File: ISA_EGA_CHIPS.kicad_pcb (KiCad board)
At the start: 2 copper layers, 131.1 x 108 mm, 67 parts, among them J1 EGA Feature Connector, J2 Light Pen, J3 RCA 1, J4 RCA 2, J6 Digital Output, J7 Bus_ISA_8bit, SW1 Configuration, U1 41464, U10 27C256, U11 82A436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

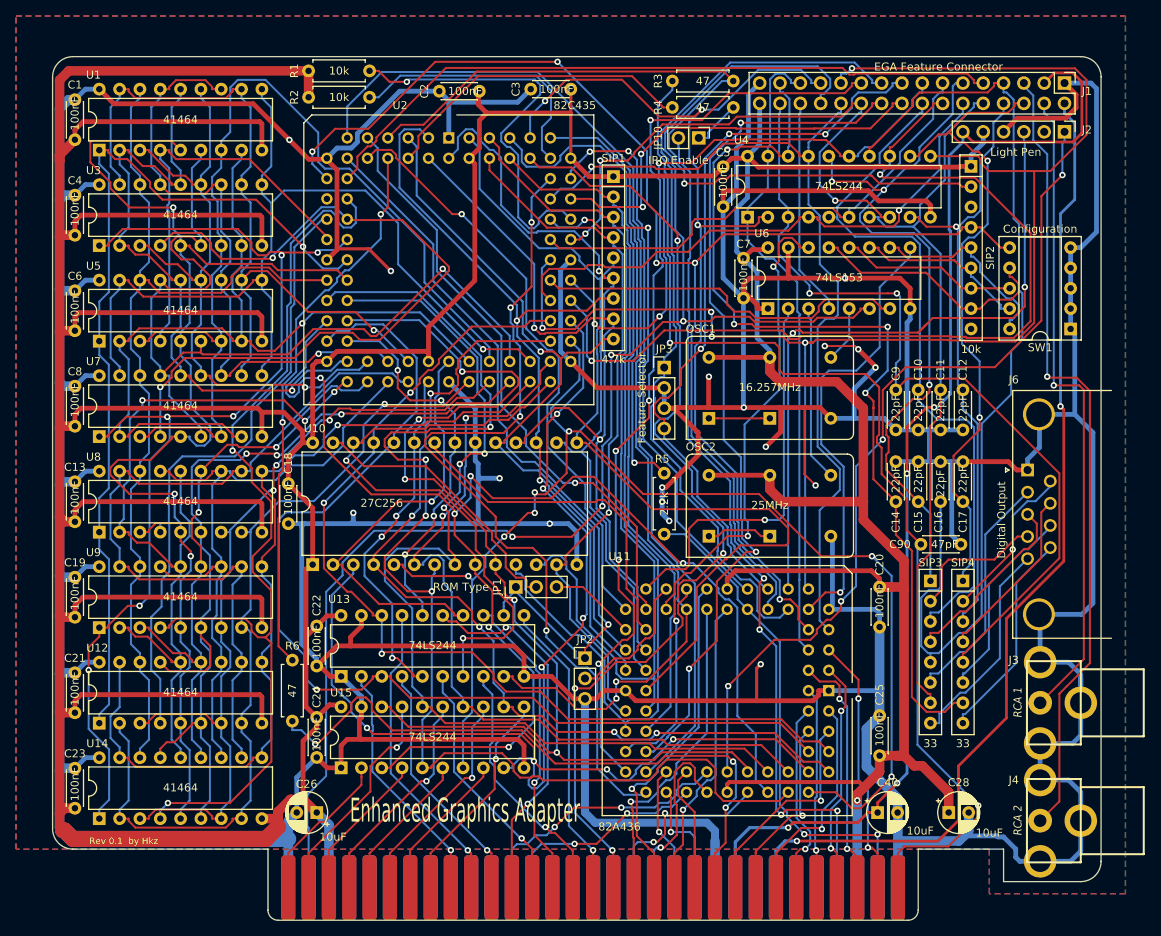
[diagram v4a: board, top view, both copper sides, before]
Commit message: Update grounding
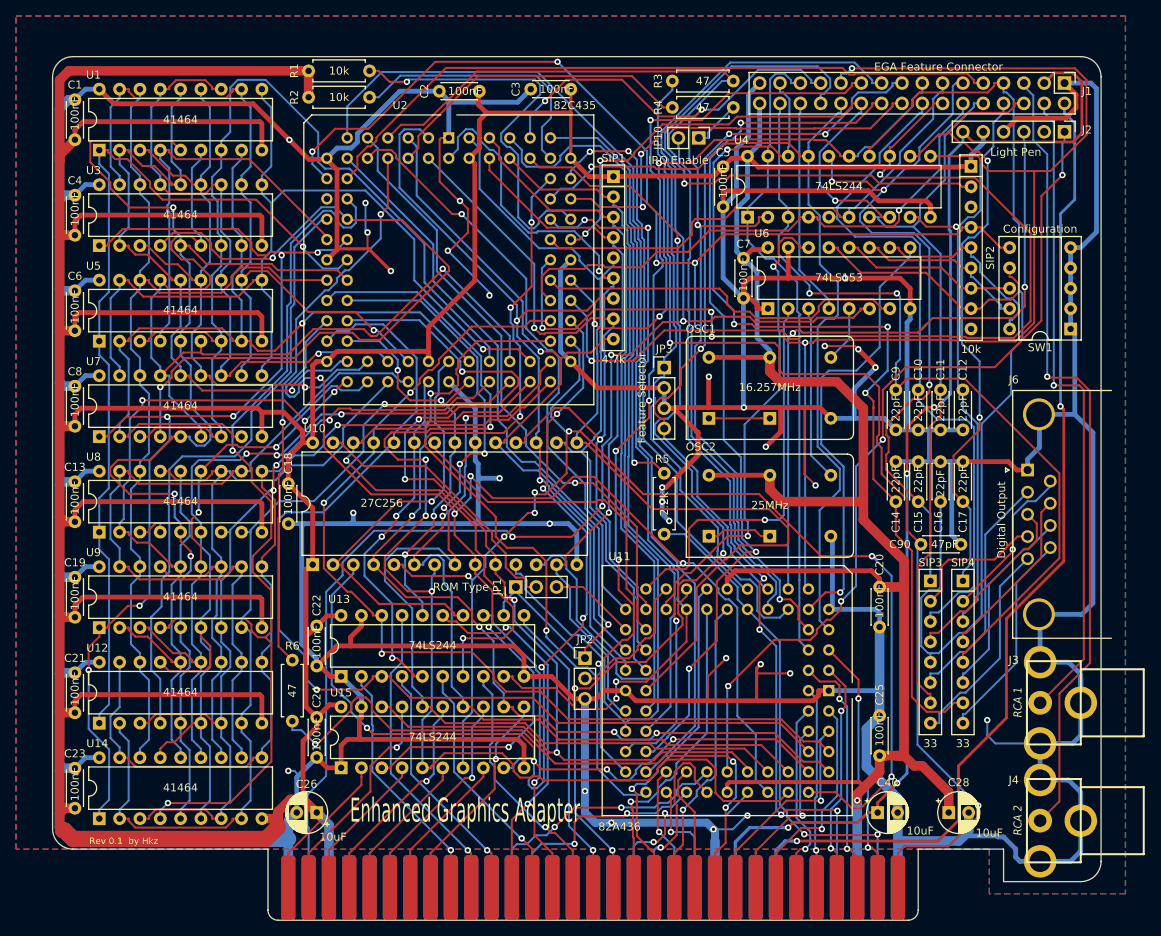
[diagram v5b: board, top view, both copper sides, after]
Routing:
- net GND: track 1036.8 -> 1094.3 mm, vias 17 -> 30
- net /~DACK0: track 26.8 -> 28.4 mm
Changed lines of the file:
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@@
     (thickness 1.6)
     (drawings 22)
-    (tracks 4128)
+    (tracks 4179)
     (zones 0)
     (modules 67)
@@
   (segment (start 243.666 99.568) (end 242.0386 101.1954) (width 0.6) (layer B.Cu) (net 1))
   (segment (start 242.0386 101.1954) (end 233.426 101.1954) (width 0.6) (layer B.Cu) (net 1))
-  (segment (start 216.916 183.104) (end 214.416 185.604) (width 0.6) (layer B.Cu) (net 1))
   (segment (start 214.416 185.604) (end 214.416 189.992) (width 0.6) (layer B.Cu) (net 1))
   (segment (start 255.524 174.752) (end 256.79 176.018) (width 0.6) (layer F.Cu) (net 1))
@@
   (segment (start 311.15 127) (end 311.15 124.46) (width 0.6) (layer B.Cu) (net 1))
   (segment (start 266.7 193.548) (end 266.7 192.278) (width 1) (layer B.Cu) (net 1))
-  (segment (start 266.7 192.278) (end 265.684 191.262) (width 1) (layer B.Cu) (net 1))
-  (segment (start 265.684 191.262) (end 251.714 191.262) (width 1) (layer B.Cu) (net 1))
+  (segment (start 266.7 192.278) (end 266.5095 192.0875) (width 1) (layer B.Cu) (net 1))
+  (segment (start 265.684 191.262) (end 253.746 191.262) (width 1) (layer B.Cu) (net 1))
   (segment (start 251.714 191.262) (end 250.444 189.992) (width 1) (layer B.Cu) (net 1))
-  (segment (start 250.444 189.992) (end 250.444 175.768) (width 1) (layer B.Cu) (net 1))
+  (segment (start 250.444 189.992) (end 250.444 187.325) (width 1) (layer B.Cu) (net 1))
   (segment (start 297.688 142.16) (end 294.894 142.16) (width 0.6) (layer B.Cu) (net 1))
   (segment (start 287.274 177.88) (end 287.274 174.498) (width 1.2) (layer B.Cu) (net 1))
@@
   (via (at 272.415 171.45) (size 0.8) (drill 0.4) (layers F.Cu B.Cu) (net 1))
   (segment (start 271.903 171.962) (end 272.415 171.45) (width 0.4) (layer F.Cu) (net 1))
-  (segment (start 271.903 176.018) (end 271.903 171.962) (width 0.4) (layer F.Cu) (net 1))
-  (segment (start 256.79 176.018) (end 271.903 176.018) (width 0.6) (layer F.Cu) (net 1))
   (segment (start 271.903 176.018) (end 278.9485 176.018) (width 0.6) (layer F.Cu) (net 1))
   (segment (start 213.4944 105.9106) (end 215.9188 108.335) (width 0.6) (layer F.Cu) (net 1))
@@
   (segment (start 277.876 139.446) (end 277.7956 139.3656) (width 0.25) (layer F.Cu) (net 1))
   (segment (start 279.8276 139.3656) (end 277.7956 139.3656) (width 0.6) (layer F.Cu) (net 1))
+  (via (at 223.266 117.475) (size 0.8) (drill 0.4) (layers F.Cu B.Cu) (net 1))
+  (segment (start 223.266 119.38) (end 223.411201 119.525201) (width 0.25) (layer F.Cu) (net 1))
+  (segment (start 223.266 117.475) (end 223.266 119.38) (width 0.25) (layer F.Cu) (net 1))
+  (via (at 223.012 113.792) (size 0.8) (drill 0.4) (layers F.Cu B.Cu) (net 1))
+  (segment (start 223.012 117.221) (end 223.266 117.475) (width 0.25) (layer B.Cu) (net 1))
+  (segment (start 223.012 113.792) (end 223.012 117.221) (width 0.25) (layer B.Cu) (net 1))
+  (segment (start 232.4648 105.664) (end 232.283 105.8458) (width 0.25) (layer F.Cu) (net 1))
+  (segment (start 233.426 105.664) (end 232.4648 105.664) (width 0.25) (layer F.Cu) (net 1))
+  (segment (start 232.283 105.8458) (end 232.283 111.125) (width 0.25) (layer F.Cu) (net 1))
+  (via (at 234.823 113.538) (size 0.8) (drill 0.4) (layers F.Cu B.Cu) (net 1))
+  (segment (start 234.696 113.538) (end 234.823 113.538) (width 0.25) (layer F.Cu) (net 1))
+  (segment (start 232.283 111.125) (end 234.696 113.538) (width 0.25) (layer F.Cu) (net 1))
+  (segment (start 235.810301 114.525301) (end 235.810301 117.503699) (width 0.25) (layer F.Cu) (net 1))
+  (segment (start 234.823 113.538) (end 235.810301 114.525301) (width 0.25) (layer F.Cu) (net 1))
+  (via (at 233.299 119.761) (size 0.8) (drill 0.4) (layers F.Cu B.Cu) (net 1))
+  (segment (start 233.553 119.761) (end 233.299 119.761) (width 0.25) (layer F.Cu) (net 1))
+  (segment (start 235.810301 117.503699) (end 233.553 119.761) (width 0.25) (layer F.Cu) (net 1))
+  (via (at 238.506 125.349) (size 0.8) (drill 0.4) (layers F.Cu B.Cu) (net 1))
+  (segment (start 238.506 124.968) (end 238.506 125.349) (width 0.25) (layer B.Cu) (net 1))
+  (segment (start 233.299 119.761) (end 238.506 124.968) (width 0.25) (layer B.Cu) (net 1))
+  (via (at 276.098 172.593) (size 0.8) (drill 0.4) (layers F.Cu B.Cu) (net 1))
+  (via (at 268.097 170.688) (size 0.8) (drill 0.4) (layers F.Cu B.Cu) (net 1))
+  (segment (start 272.026 172.593) (end 271.903 172.47) (width 0.25) (layer F.Cu) (net 1))
+  (segment (start 276.098 172.593) (end 272.026 172.593) (width 0.25) (layer F.Cu) (net 1))
+  (segment (start 271.903 172.47) (end 271.903 171.962) (width 0.4) (layer F.Cu) (net 1))
+  (segment (start 271.903 176.018) (end 271.903 172.47) (width 0.4) (layer F.Cu) (net 1))
+  (segment (start 268.097 170.688) (end 265.811 172.974) (width 0.25) (layer F.Cu) (net 1))
+  (segment (start 265.811 175.895) (end 265.688 176.018) (width 0.25) (layer F.Cu) (net 1))
+  (segment (start 265.811 172.974) (end 265.811 175.895) (width 0.25) (layer F.Cu) (net 1))
+  (segment (start 265.688 176.018) (end 271.903 176.018) (width 0.6) (layer F.Cu) (net 1))
+  (segment (start 256.79 176.018) (end 265.688 176.018) (width 0.6) (layer F.Cu) (net 1))
+  (segment (start 250.444 187.325) (end 250.444 175.768) (width 1) (layer B.Cu) (net 1))
+  (via (at 250.444 187.325) (size 0.8) (drill 0.4) (layers F.Cu B.Cu) (net 1))
+  (segment (start 266.5095 192.0875) (end 265.684 191.262) (width 1) (layer B.Cu) (net 1))
+  (via (at 266.5095 192.0875) (size 0.8) (drill 0.4) (layers F.Cu B.Cu) (net 1))
+  (via (at 270.764 190.373) (size 0.8) (drill 0.4) (layers F.Cu B.Cu) (net 1))
+  (segment (start 266.5095 192.0875) (end 268.9225 192.0875) (width 0.25) (layer B.Cu) (net 1))
+  (segment (start 270.637 190.373) (end 270.764 190.373) (width 0.25) (layer B.Cu) (net 1))
+  (segment (start 268.9225 192.0875) (end 270.637 190.373) (width 0.25) (layer B.Cu) (net 1))
+  (segment (start 253.746 191.262) (end 251.714 191.262) (width 1) (layer B.Cu) (net 1))
+  (via (at 253.746 191.262) (size 0.8) (drill 0.4) (layers F.Cu B.Cu) (net 1))
+  (via (at 213.36 184.785) (size 0.8) (drill 0.4) (layers F.Cu B.Cu) (net 1))
+  (segment (start 214.122 184.785) (end 214.6785 185.3415) (width 0.25) (layer B.Cu) (net 1))
+  (segment (start 213.36 184.785) (end 214.122 184.785) (width 0.25) (layer B.Cu) (net 1))
+  (segment (start 214.6785 185.3415) (end 214.416 185.604) (width 0.6) (layer B.Cu) (net 1))
+  (segment (start 216.916 183.104) (end 214.6785 185.3415) (width 0.6) (layer B.Cu) (net 1))
+  (via (at 300.736 178.435) (size 0.8) (drill 0.4) (layers F.Cu B.Cu) (net 1))
+  (segment (start 300.736 178.435) (end 300.736 180.34) (width 0.25) (layer B.Cu) (net 1))
+  (segment (start 301.752 181.356) (end 307.34 181.356) (width 0.25) (layer B.Cu) (net 1))
+  (segment (start 300.736 180.34) (end 301.752 181.356) (width 0.25) (layer B.Cu) (net 1))
   (segment (start 297.3537 109.22) (end 297.2594 109.3143) (width 0.6) (layer F.Cu) (net 2))
   (segment (start 297.2594 109.3143) (end 287.7666 109.3143) (width 0.6) (layer F.Cu) (net 2))
@@
   (segment (start 256.54 194.183) (end 256.54 199.39) (width 0.25) (layer B.Cu) (net 48))
   (segment (start 257.0362 193.6868) (end 256.54 194.183) (width 0.25) (layer B.Cu) (net 48))
-  (segment (start 249.1459 193.9087) (end 251.8891 193.9087) (width 0.25) (layer F.Cu) (net 49))
-  (segment (start 251.8891 193.9087) (end 255.7155 190.0823) (width 0.25) (layer F.Cu) (net 49))
   (segment (start 255.7155 190.0823) (end 259.3203 190.0823) (width 0.25) (layer B.Cu) (net 49))
   (segment (start 259.3203 190.0823) (end 260.125 189.2776) (width 0.25) (layer B.Cu) (net 49))
@@
   (via (at 255.7155 190.0823) (size 0.8) (layers F.Cu B.Cu) (net 49))
   (via (at 249.1459 193.9087) (size 0.8) (layers F.Cu B.Cu) (net 49))
+  (segment (start 255.315501 190.482299) (end 249.826701 190.482299) (width 0.25) (layer F.Cu) (net 49))
+  (segment (start 255.7155 190.0823) (end 255.315501 190.482299) (width 0.25) (layer F.Cu) (net 49))
+  (segment (start 249.1459 191.1631) (end 249.1459 193.9087) (width 0.25) (layer F.Cu) (net 49))
+  (segment (start 249.826701 190.482299) (end 249.1459 191.1631) (width 0.25) (layer F.Cu) (net 49))
   (segment (start 246.665 191.7993) (end 249.0884 189.3759) (width 0.25) (layer F.Cu) (net 50))
   (segment (start 249.0884 189.3759) (end 254.9906 189.3759) (width 0.25) (layer F.Cu) (net 50))
@@
   (segment (start 211.2439 113.8172) (end 212.8217 112.2394) (width 0.25) (layer B.Cu) (net 119))
   (segment (start 212.8217 112.2394) (end 222.9884 112.2394) (width 0.25) (layer B.Cu) (net 119))
-  (segment (start 222.9884 112.2394) (end 227.0918 116.3428) (width 0.25) (layer B.Cu) (net 119))
-  (segment (start 227.0918 116.3428) (end 227.0918 121.4583) (width 0.25) (layer B.Cu) (net 119))
-  (segment (start 227.0918 121.4583) (end 237.7116 132.0781) (width 0.25) (layer B.Cu) (net 119))
   (segment (start 211.2439 113.8172) (end 211.2439 119.8061) (width 0.25) (layer B.Cu) (net 119))
   (segment (start 211.2439 119.8061) (end 210.058 120.992) (width 0.25) (layer B.Cu) (net 119))
@@
   (segment (start 210.058 123.444) (end 210.058 122.3187) (width 0.25) (layer B.Cu) (net 119))
   (via (at 237.7116 132.0781) (size 0.8) (layers F.Cu B.Cu) (net 119))
+  (segment (start 237.7116 132.0781) (end 229.108 123.4745) (width 0.25) (layer B.Cu) (net 119))
+  (segment (start 229.108 118.359) (end 227.015 116.266) (width 0.25) (layer B.Cu) (net 119))
+  (segment (start 229.108 123.4745) (end 229.108 118.359) (width 0.25) (layer B.Cu) (net 119))
+  (segment (start 227.015 116.266) (end 227.0918 116.3428) (width 0.25) (layer B.Cu) (net 119))
+  (segment (start 222.9884 112.2394) (end 227.015 116.266) (width 0.25) (layer B.Cu) (net 119))
   (segment (start 220.726 120.904) (end 219.6394 121.9906) (width 0.25) (layer B.Cu) (net 120))
   (segment (start 219.6394 121.9906) (end 217.685 121.9906) (width 0.25) (layer B.Cu) (net 120))

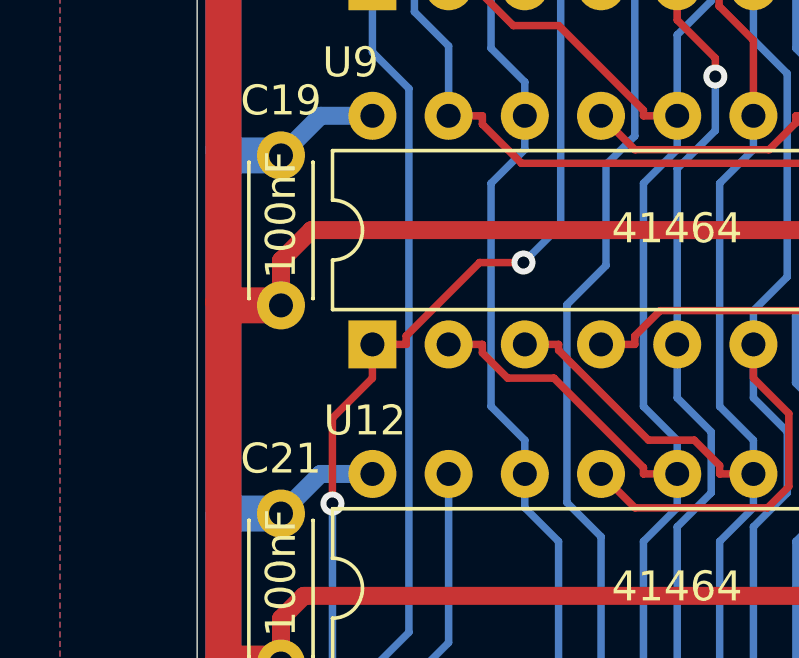
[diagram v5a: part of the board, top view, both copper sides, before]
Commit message: Add more grounding
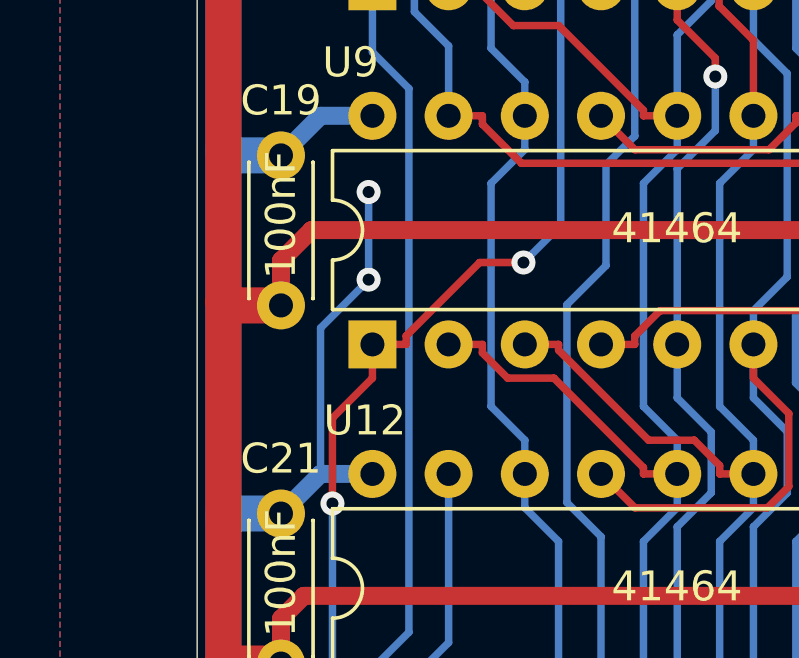
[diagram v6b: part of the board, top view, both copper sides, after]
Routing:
- net GND: track 1094.3 -> 1104.4 mm, vias 30 -> 32
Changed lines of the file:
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@@
     (thickness 1.6)
     (drawings 22)
-    (tracks 4179)
+    (tracks 4185)
     (zones 0)
     (modules 67)
@@
   (segment (start 301.752 181.356) (end 307.34 181.356) (width 0.25) (layer B.Cu) (net 1))
   (segment (start 300.736 180.34) (end 301.752 181.356) (width 0.25) (layer B.Cu) (net 1))
+  (via (at 189.611 164.719) (size 0.8) (drill 0.4) (layers F.Cu B.Cu) (net 1))
+  (segment (start 189.611 164.729998) (end 189.611 164.719) (width 0.25) (layer B.Cu) (net 1))
+  (segment (start 188.01 166.330998) (end 189.611 164.729998) (width 0.25) (layer B.Cu) (net 1))
+  (segment (start 188.01 171.196) (end 188.01 166.330998) (width 0.25) (layer B.Cu) (net 1))
+  (segment (start 189.611 164.719) (end 189.611 161.798) (width 0.25) (layer B.Cu) (net 1))
+  (via (at 189.611 161.798) (size 0.8) (drill 0.4) (layers F.Cu B.Cu) (net 1))
   (segment (start 297.3537 109.22) (end 297.2594 109.3143) (width 0.6) (layer F.Cu) (net 2))
   (segment (start 297.2594 109.3143) (end 287.7666 109.3143) (width 0.6) (layer F.Cu) (net 2))

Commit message: Add bio menace guy!
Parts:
- added LOGO: , Custom_Silkscreen:LOGO, F.Cu at (256.0, 112.1)
